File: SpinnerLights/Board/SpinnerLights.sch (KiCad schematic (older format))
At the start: 14 parts, among them U1 SeeeduinoXIAO, U2 ADXL343

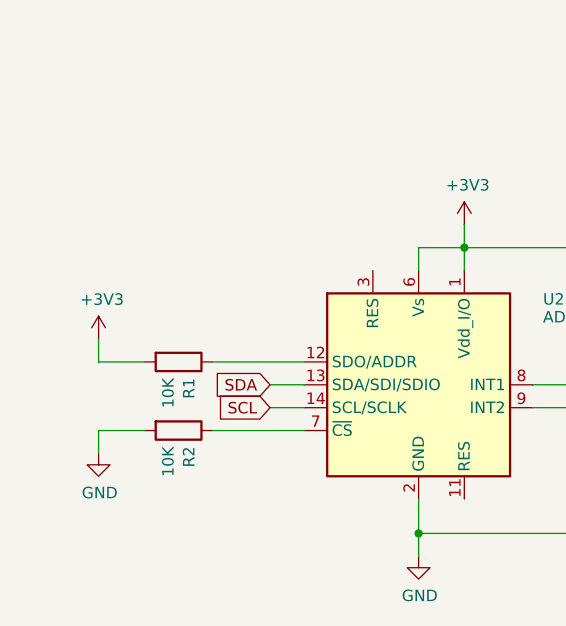
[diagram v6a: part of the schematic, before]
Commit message: SpinnerLights: Fix I2C interface pins
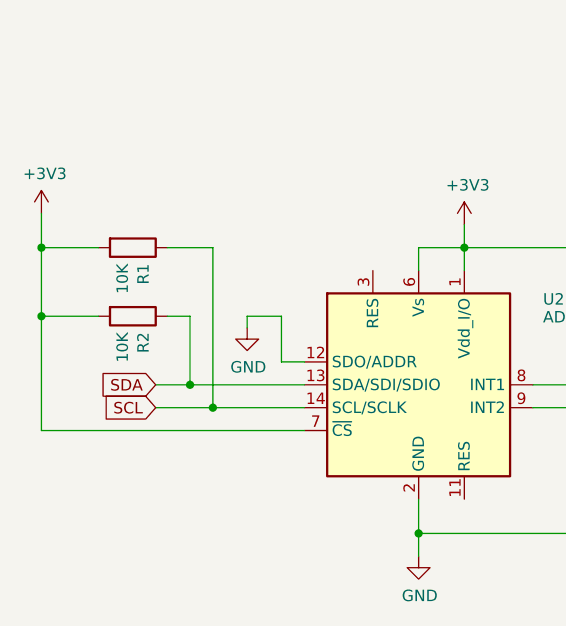
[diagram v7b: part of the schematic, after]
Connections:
- net +3V3: now also R2.2, U2.7 (~CS)
- net GND: now also U2.12 (SDO/ADDR); no longer R2.2
- net SCL: now also R1.1
- net SDA: now also R2.1
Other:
- moved on the sheet: R1, R2
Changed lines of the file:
@@
 	1    0    0    -1
 $EndComp
-Wire Wire Line
-	1800 4550 1800 4650
-Wire Wire Line
-	2000 4550 1800 4550
-Wire Wire Line
-	2700 4550 2300 4550
 $Comp
 L Device:R R2
 U 1 1 6176EC78
-P 2150 4550
-F 0 "R2" H 2220 4596 50  0000 L CNN
-F 1 "10K" H 2220 4505 50  0000 L CNN
-F 2 "Resistor_SMD:R_0805_2012Metric_Pad1.20x1.40mm_HandSolder" V 2080 4550 50  0001 C CNN
-F 3 "~" H 2150 4550 50  0001 C CNN
-	1    2150 4550
+P 1950 4050
+F 0 "R2" H 2020 4096 50  0000 L CNN
+F 1 "10K" H 2020 4005 50  0000 L CNN
+F 2 "Resistor_SMD:R_0805_2012Metric_Pad1.20x1.40mm_HandSolder" V 1880 4050 50  0001 C CNN
+F 3 "~" H 1950 4050 50  0001 C CNN
+	1    1950 4050
 	0    1    1    0
 $EndComp
 Wire Wire Line
-	1800 4250 1800 4150
+	2050 4350 2200 4350
 Wire Wire Line
-	2550 4350 2700 4350
-Wire Wire Line
-	2700 4450 2550 4450
-Text GLabel 2550 4450 0    50   Input ~ 0
+	2700 4450 2300 4450
+Text GLabel 2050 4450 0    50   Input ~ 0
 SCL
-Text GLabel 2550 4350 0    50   Input ~ 0
+Text GLabel 2050 4350 0    50   Input ~ 0
 SDA
 Wire Wire Line
@@
 Wire Wire Line
 	3700 4350 3850 4350
-$Comp
-L Sensor_Motion:ADXL343 U2
-U 1 1 61662620
-P 3200 4350
-F 0 "U2" H 3744 4724 50  0000 L CNN
-F 1 "ADXL343" H 3744 4646 50  0000 L CNN
-F 2 "Package_LGA:LGA-14_3x5mm_P0.8mm_LayoutBorder1x6y" H 3200 4350 50  0001 C CNN
-F 3 "https://www.analog.com/media/en/technical-documentation/data-sheets/ADXL343.pdf" H 3200 4350 50  0001 C CNN
-	1    3200 4350
-	1    0    0    -1
-$EndComp
 Text GLabel 3850 4350 2    50   Input ~ 0
 INT1
@@
 	1    0    0    -1
 $EndComp
-Wire Wire Line
-	2300 4250 2700 4250
-Wire Wire Line
-	2000 4250 1800 4250
 $Comp
 L power:+3V3 #PWR02
 U 1 1 6166C856
-P 1800 4150
-F 0 "#PWR02" H 1800 4000 50  0001 C CNN
-F 1 "+3V3" H 1815 4323 50  0000 C CNN
-F 2 "" H 1800 4150 50  0001 C CNN
-F 3 "" H 1800 4150 50  0001 C CNN
-	1    1800 4150
+P 1550 3600
+F 0 "#PWR02" H 1550 3450 50  0001 C CNN
+F 1 "+3V3" H 1565 3773 50  0000 C CNN
+F 2 "" H 1550 3600 50  0001 C CNN
+F 3 "" H 1550 3600 50  0001 C CNN
+	1    1550 3600
 	1    0    0    -1
 $EndComp
@@
 L Device:R R1
 U 1 1 6166A991
-P 2150 4250
-F 0 "R1" H 2220 4296 50  0000 L CNN
-F 1 "10K" H 2220 4205 50  0000 L CNN
-F 2 "Resistor_SMD:R_0805_2012Metric_Pad1.20x1.40mm_HandSolder" V 2080 4250 50  0001 C CNN
-F 3 "~" H 2150 4250 50  0001 C CNN
-	1    2150 4250
+P 1950 3750
+F 0 "R1" H 2020 3796 50  0000 L CNN
+F 1 "10K" H 2020 3705 50  0000 L CNN
+F 2 "Resistor_SMD:R_0805_2012Metric_Pad1.20x1.40mm_HandSolder" V 1880 3750 50  0001 C CNN
+F 3 "~" H 1950 3750 50  0001 C CNN
+	1    1950 3750
 	0    1    1    0
 $EndComp
@@
 L power:GND #PWR01
 U 1 1 616648C6
-P 1800 4650
-F 0 "#PWR01" H 1800 4400 50  0001 C CNN
-F 1 "GND" H 1805 4477 50  0000 C CNN
-F 2 "" H 1800 4650 50  0001 C CNN
-F 3 "" H 1800 4650 50  0001 C CNN
-	1    1800 4650
+P 2450 4100
+F 0 "#PWR01" H 2450 3850 50  0001 C CNN
+F 1 "GND" H 2455 3927 50  0000 C CNN
+F 2 "" H 2450 4100 50  0001 C CNN
+F 3 "" H 2450 4100 50  0001 C CNN
+	1    2450 4100
 	1    0    0    -1
 $EndComp
@@
 Wire Wire Line
 	10050 3000 9850 3000
+Wire Wire Line
+	1550 4550 1550 4050
+Wire Wire Line
+	1550 4550 2700 4550
+Wire Wire Line
+	2200 4350 2200 4050
+Wire Wire Line
+	2200 4050 2100 4050
+Connection ~ 2200 4350
+Wire Wire Line
+	2200 4350 2700 4350
+Wire Wire Line
+	2300 4450 2300 3750
+Wire Wire Line
+	2300 3750 2100 3750
+Connection ~ 2300 4450
+Wire Wire Line
+	2300 4450 2050 4450
+Wire Wire Line
+	1800 3750 1550 3750
+Connection ~ 1550 3750
+Wire Wire Line
+	1550 3750 1550 3600
+Wire Wire Line
+	1800 4050 1550 4050
+Connection ~ 1550 4050
+Wire Wire Line
+	1550 4050 1550 3750
+$Comp
+L Sensor_Motion:ADXL343 U2
+U 1 1 61662620
+P 3200 4350
+F 0 "U2" H 3744 4724 50  0000 L CNN
+F 1 "ADXL343" H 3744 4646 50  0000 L CNN
+F 2 "Package_LGA:LGA-14_3x5mm_P0.8mm_LayoutBorder1x6y" H 3200 4350 50  0001 C CNN
+F 3 "https://www.analog.com/media/en/technical-documentation/data-sheets/ADXL343.pdf" H 3200 4350 50  0001 C CNN
+	1    3200 4350
+	1    0    0    -1
+$EndComp
+Wire Wire Line
+	2600 4050 2450 4050
+Wire Wire Line
+	2700 4250 2600 4250
+Wire Wire Line
+	2600 4250 2600 4050
+Wire Wire Line
+	2450 4050 2450 4100
 $EndSCHEMATC

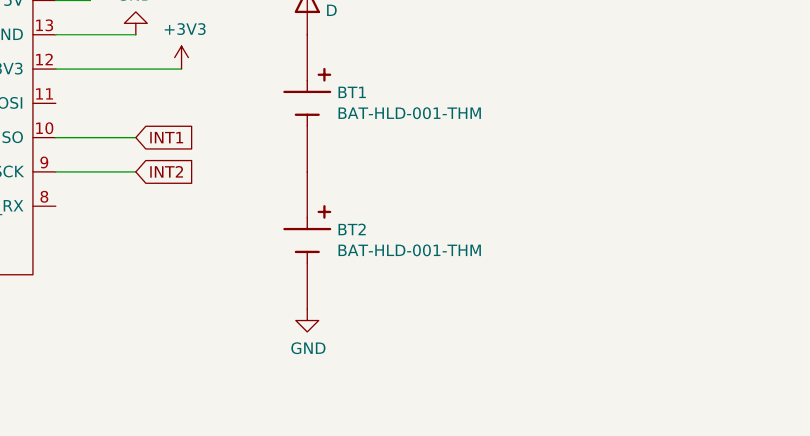
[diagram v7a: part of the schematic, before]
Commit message: SpinnerLights: Rename a couple nets
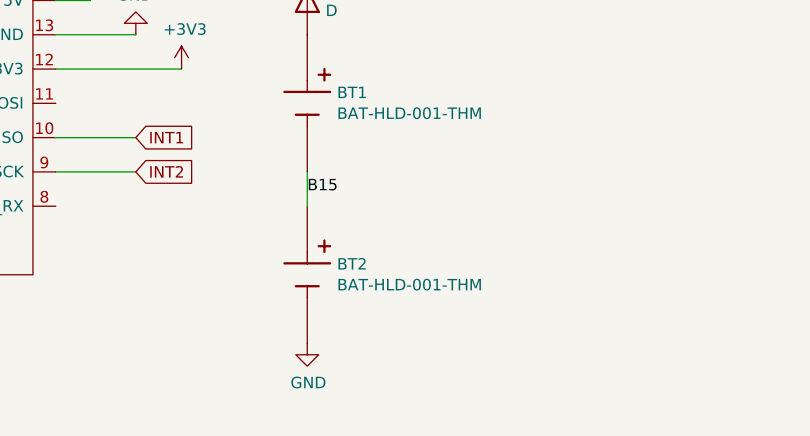
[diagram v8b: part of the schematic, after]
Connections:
- net B15: now reaches BT1.N, BT2.P1, BT2.P2, BT2.P3, BT2.P4
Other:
- moved on the sheet: BT2
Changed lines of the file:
@@
 L BAT-HLD-001-THM:BAT-HLD-001-THM BT2
 U 1 1 617077E9
-P 8200 4550
-F 0 "BT2" V 8154 4680 50  0000 L CNN
-F 1 "BAT-HLD-001-THM" V 8245 4680 50  0000 L CNN
-F 2 "BAT-HLD-001-THM:BAT_BAT-HLD-001-THM" H 8200 4550 50  0001 L BNN
-F 3 "" H 8200 4550 50  0001 L BNN
-F 4 "Manufacturer Recommendations" H 8200 4550 50  0001 L BNN "STANDARD"
-F 5 "C" H 8200 4550 50  0001 L BNN "PARTREV"
-F 6 "Linx Technologies" H 8200 4550 50  0001 L BNN "MANUFACTURER"
-F 7 "4.2mm" H 8200 4550 50  0001 L BNN "MAXIMUM_PACKAGE_HEIGHT"
-	1    8200 4550
+P 8200 4700
+F 0 "BT2" V 8154 4830 50  0000 L CNN
+F 1 "BAT-HLD-001-THM" V 8245 4830 50  0000 L CNN
+F 2 "BAT-HLD-001-THM:BAT_BAT-HLD-001-THM" H 8200 4700 50  0001 L BNN
+F 3 "" H 8200 4700 50  0001 L BNN
+F 4 "Manufacturer Recommendations" H 8200 4700 50  0001 L BNN "STANDARD"
+F 5 "C" H 8200 4700 50  0001 L BNN "PARTREV"
+F 6 "Linx Technologies" H 8200 4700 50  0001 L BNN "MANUFACTURER"
+F 7 "4.2mm" H 8200 4700 50  0001 L BNN "MAXIMUM_PACKAGE_HEIGHT"
+	1    8200 4700
 	0    1    1    0
 $EndComp
@@
 L power:GND #PWR0102
 U 1 1 617929E5
-P 8200 4850
-F 0 "#PWR0102" H 8200 4600 50  0001 C CNN
-F 1 "GND" H 8205 4677 50  0000 C CNN
-F 2 "" H 8200 4850 50  0001 C CNN
-F 3 "" H 8200 4850 50  0001 C CNN
-	1    8200 4850
+P 8200 5000
+F 0 "#PWR0102" H 8200 4750 50  0001 C CNN
+F 1 "GND" H 8205 4827 50  0000 C CNN
+F 2 "" H 8200 5000 50  0001 C CNN
+F 3 "" H 8200 5000 50  0001 C CNN
+	1    8200 5000
 	1    0    0    -1
 $EndComp
@@
 Wire Wire Line
 	2450 4050 2450 4100
+Wire Wire Line
+	8200 4400 8200 4250
+Text Label 8200 4350 0    50   ~ 0
+B15
 $EndSCHEMATC
